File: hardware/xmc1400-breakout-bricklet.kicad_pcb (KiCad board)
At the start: 2 copper layers, 50 x 45 mm, 32 parts, among them P1 CON-SENSOR2, P2 BOOT, P3 CONN_01X12, P4 CONN_01X12, P5 CONN_01X12, P6 CONN_01X12, P7 CONN_02X04, U1 XMC1XXX48, U2 DRILL, U3 DRILL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

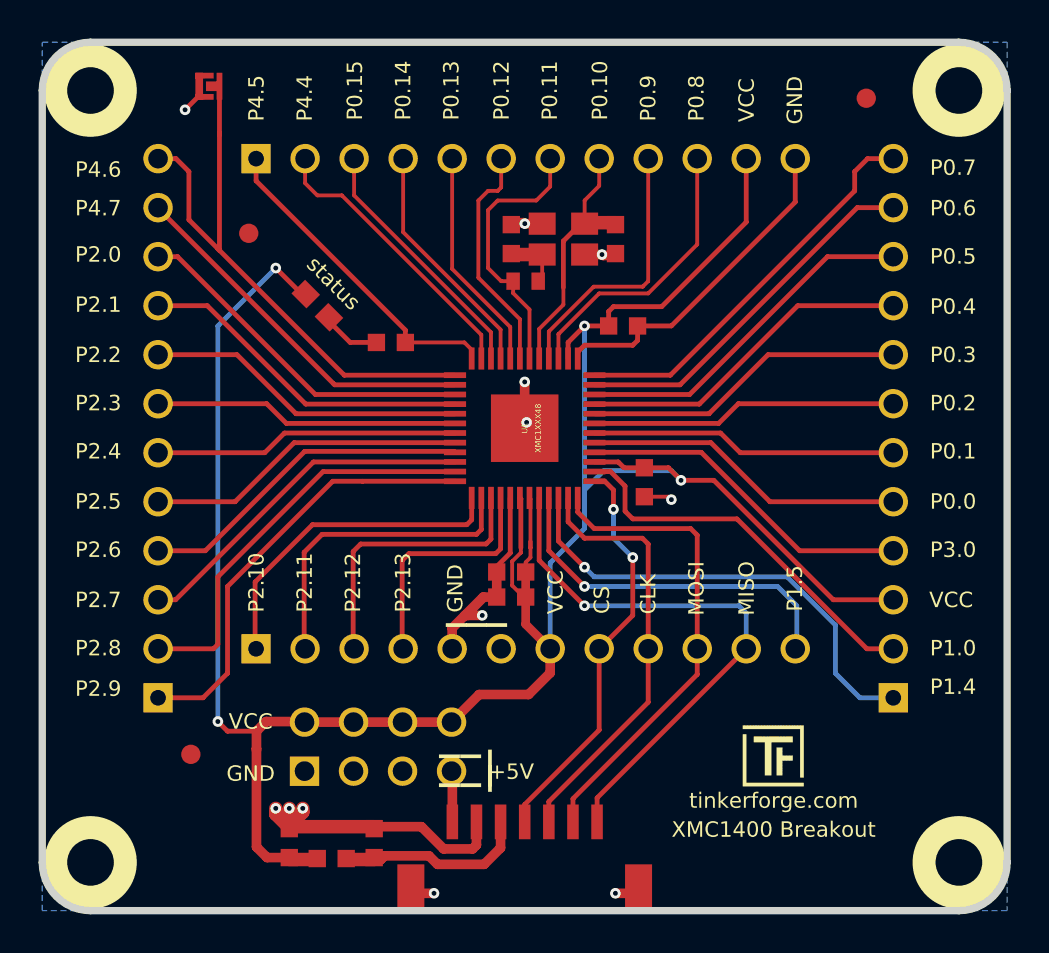
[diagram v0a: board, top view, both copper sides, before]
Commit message: added text on back silkscreen
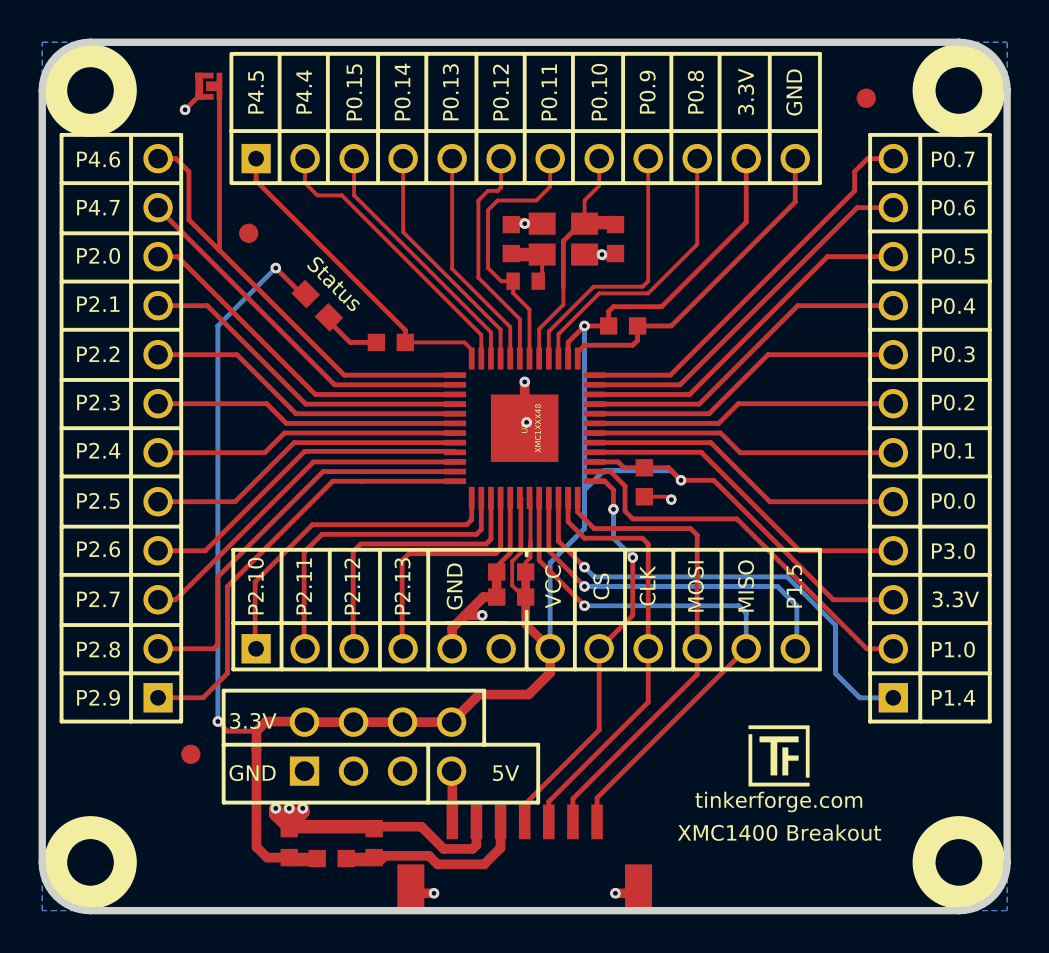
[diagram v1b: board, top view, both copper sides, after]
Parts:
- removed the VAL at (135.7, 95.1)
- added VAL: WEEE_7mm, kicad-libraries:WEEE_7mm, B.Cu at (145.4, 100.2)
- moved G*** 20.3 mm to (153.4, 100.1)
- moved VAL 3.88 mm to (137.9, 100.1)
- moved G*** 0.30 mm to (156.9, 118.5)
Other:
- board text added: "3.3V"
- board text added: "5V"
- board text added: "Status"
- board text removed: "+5V"
- board text removed: "_"
- board text removed: "status"

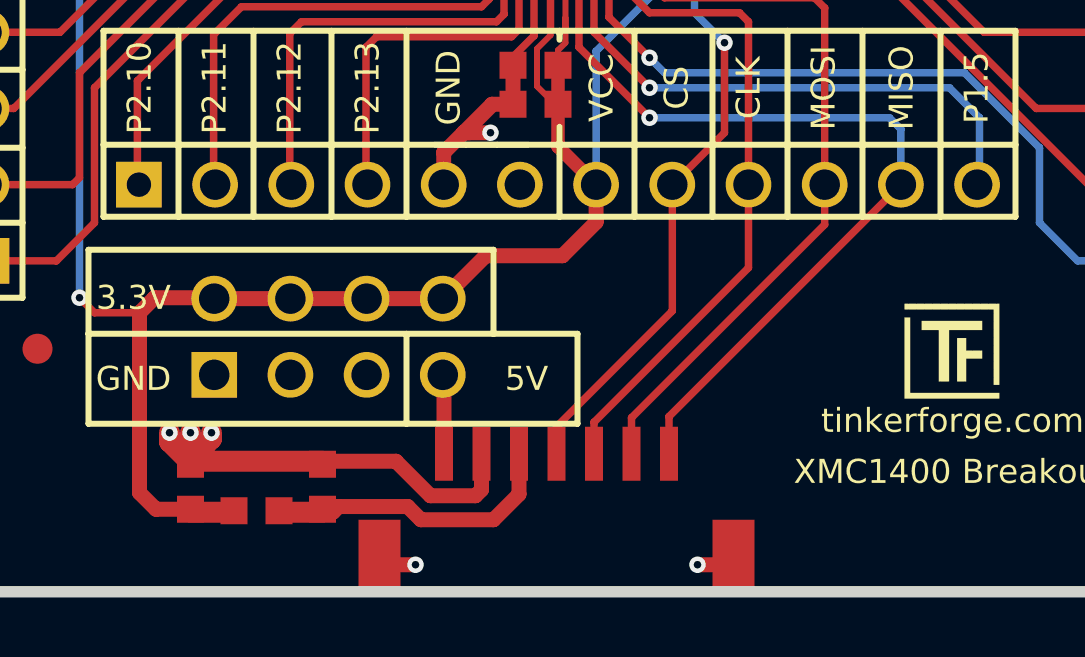
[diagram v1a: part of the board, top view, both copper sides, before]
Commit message: added filter resitor and cap in dataline
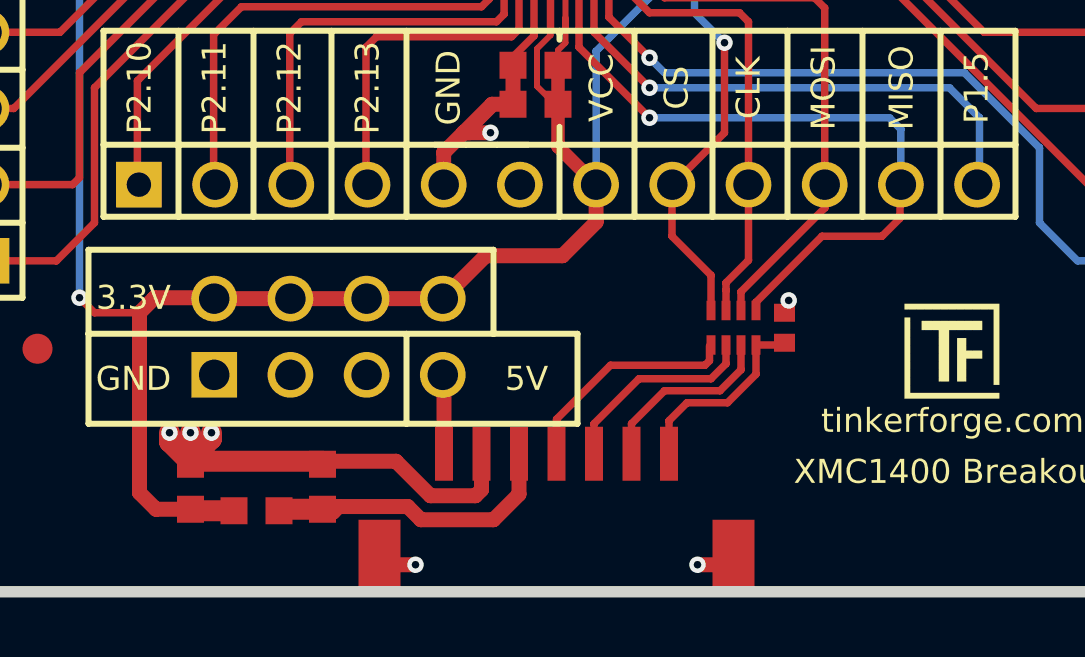
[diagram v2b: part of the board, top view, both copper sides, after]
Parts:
- added C7: 220pF, kicad-libraries:C0402F, F.Cu at (152.9, 119.3)
- added RP1: 82, kicad-libraries:4X0402, F.Cu at (151.2, 119.3)
- turned FB1 to 0 degrees
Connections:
- FB1 pad 1: Net-(C1-Pad2) -> VCC
- FB1 pad 2: VCC -> Net-(C1-Pad2)
- P1 pad 4: S-CS -> Net-(P1-Pad4)
- P1 pad 5: S-CLK -> Net-(P1-Pad5)
- P1 pad 6: S-MOSI -> Net-(P1-Pad6)
- P1 pad 7: S-MISO -> Net-(C7-Pad1)
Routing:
- net Net-(P1-Pad4): track 0.00 -> 7.56 mm
- net S-CLK: track 22.4 -> 15.8 mm
- net Net-(C7-Pad1): track 0.00 -> 6.52 mm
- net Net-(P1-Pad5): track 0.00 -> 6.25 mm
- net S-MOSI: track 24.9 -> 18.7 mm
- net Net-(P1-Pad6): track 0.00 -> 6.22 mm
- net S-CS: track 21.6 -> 15.8 mm
- net S-MISO: track 29.1 -> 24.3 mm
- net GND: track 58.6 -> 59.1 mm, vias 12 -> 13
